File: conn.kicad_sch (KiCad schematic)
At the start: 59 parts, among them J1 JST_1x02, J10 MicroFit_2x04, J11 MLX_1x03, J12 MLX_1x03, J13 JST_1x04, J14 JST_1x04, J15 JST_1x04, J16 JST_1x04, J17 JST_1x02, J5 JST_01x02, J7 JST_B6B-XH, J8 MicroFit_2x04, J9 MicroFit_2x04, SW2 !EMERG STOP!

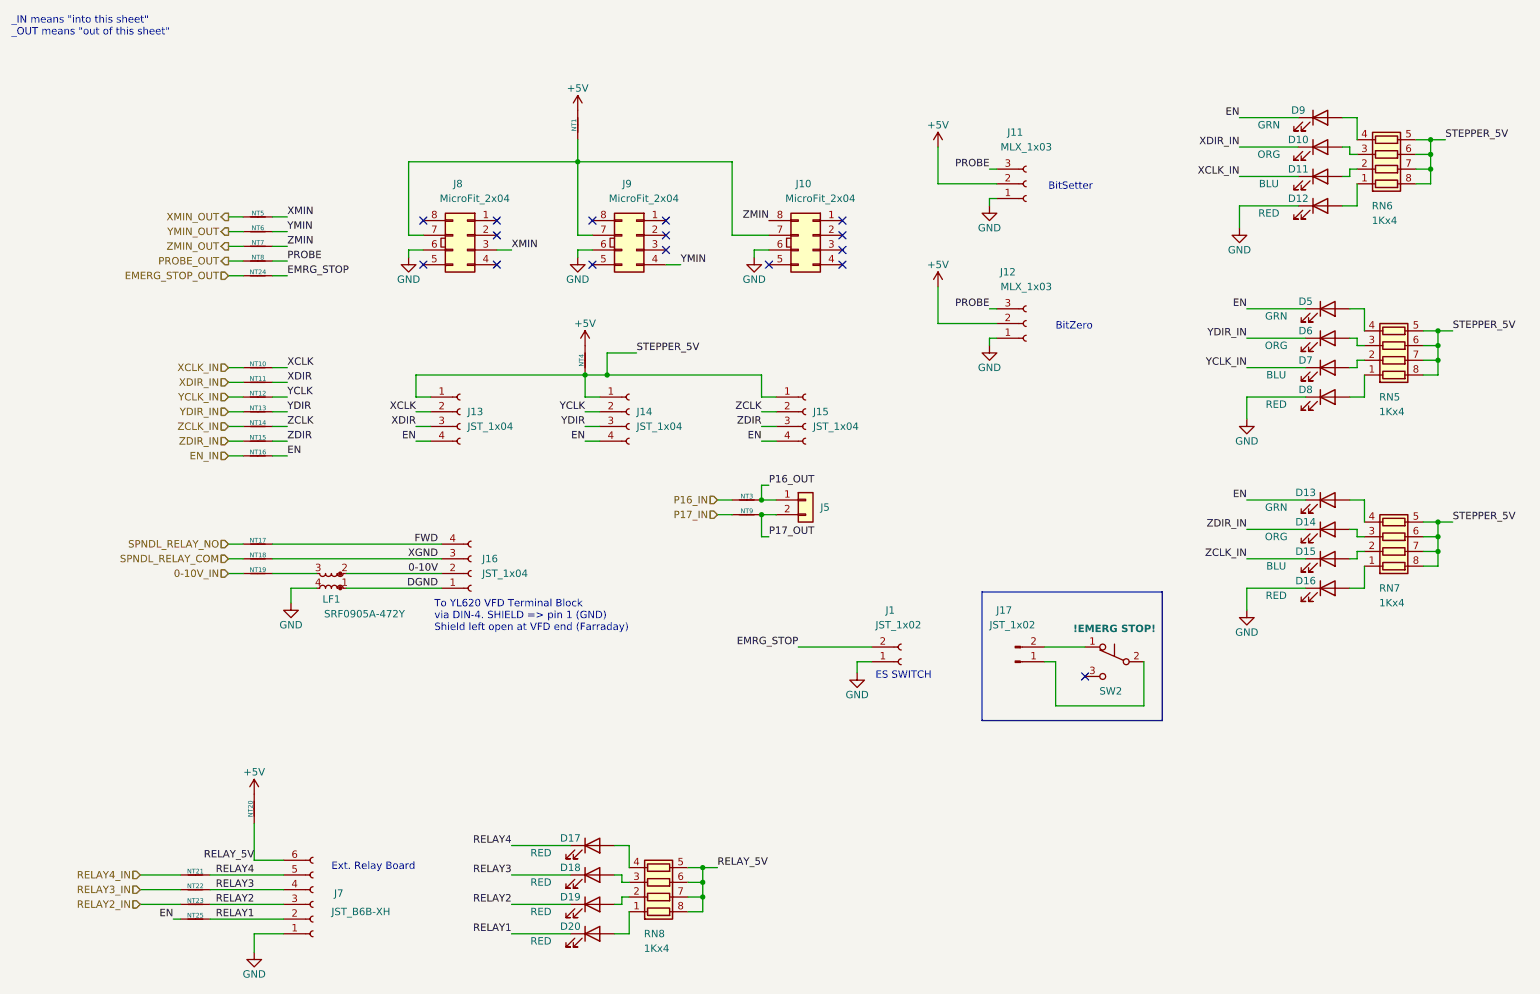
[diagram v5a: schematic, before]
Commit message: Resistor networks changed to 0603 'cause JLCPCB has those as 'basic parts' & aunch of tweaks. (WIP)
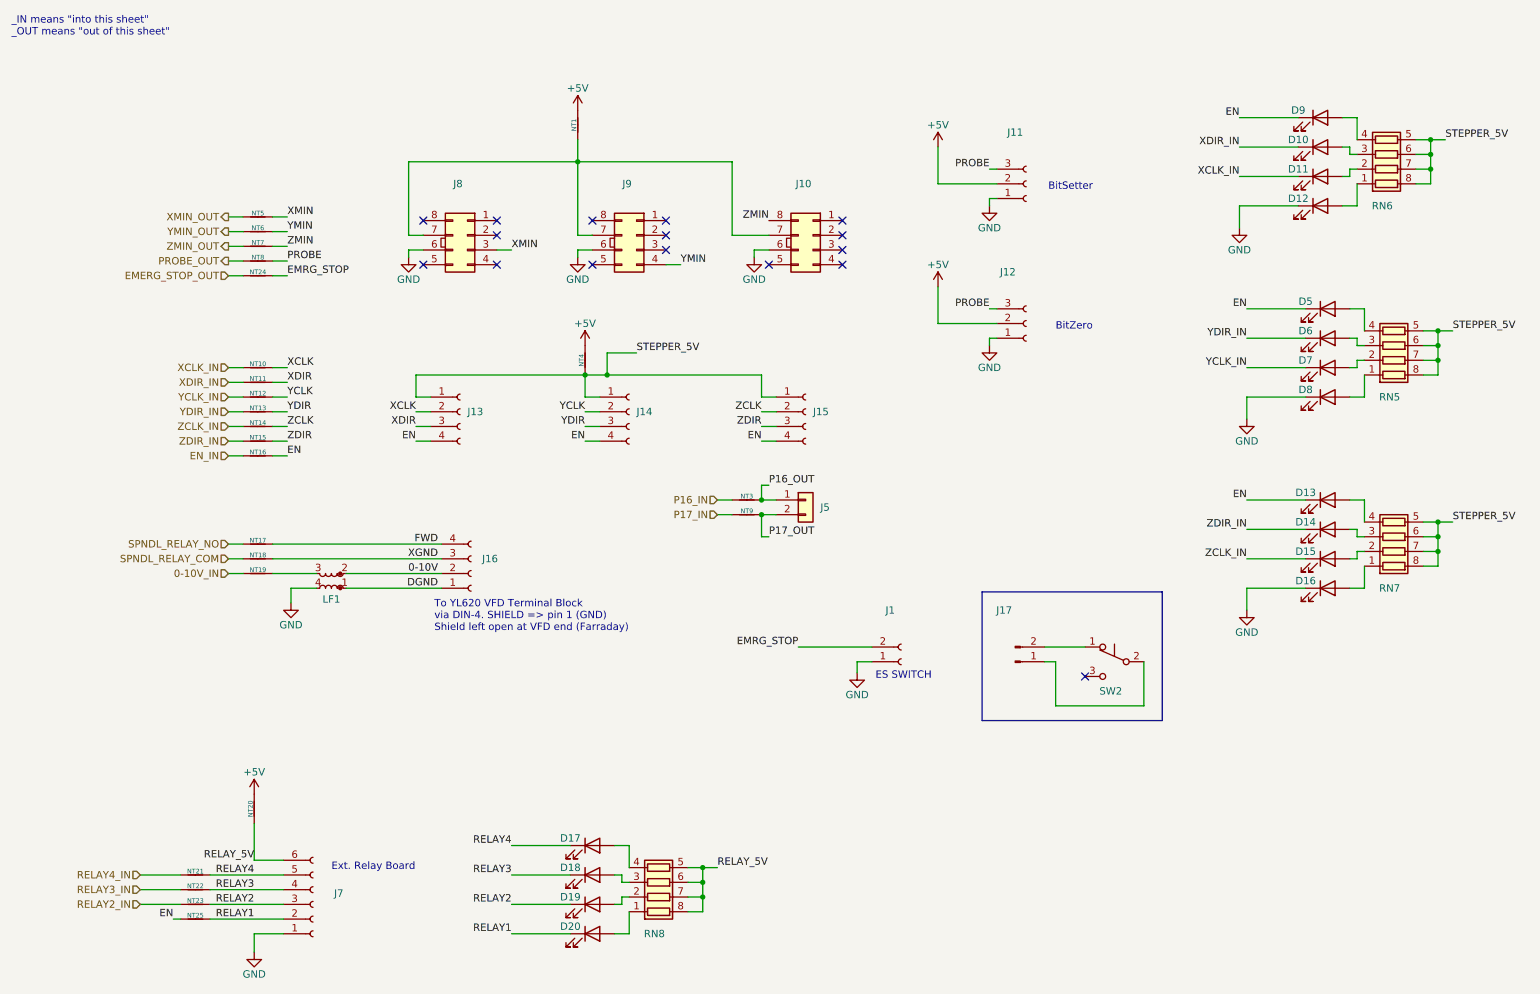
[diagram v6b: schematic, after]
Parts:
- D10, D14, D6: value ORG -> (none); footprint LED_SMD:LED_0402_1005Metric -> (none)
- D11, D15, D7: value BLU -> (none); footprint LED_SMD:LED_0402_1005Metric -> (none)
- D12, D16, D17, D18, D19, D20, D8: value RED -> (none); footprint LED_SMD:LED_0402_1005Metric -> (none)
- D13, D5, D9: value GRN -> (none); footprint LED_SMD:LED_0402_1005Metric -> (none)
- J1: value JST_1x02 -> (none); footprint Connector_JST:JST_EH_S2B-EH_1x02_P2.50mm_Horizontal -> (none)
- J10, J8, J9: value MicroFit_2x04 -> (none); footprint Connector_Molex:Molex_Micro-Fit_3.0_43045-0812_2x04_P3.00mm_Vertical -> (none)
- J11, J12: value MLX_1x03 -> (none); footprint Connector_Molex:Molex_KK-254_AE-6410-03A_1x03_P2.54mm_Vertical -> (none)
- J13, J14, J15, J16: value JST_1x04 -> (none); footprint Connector_JST:JST_EH_S4B-EH_1x04_P2.50mm_Horizontal -> (none)
- J17: value JST_1x02 -> (none); footprint Connector_Molex:Molex_KK-254_AE-6410-03A_1x02_P2.54mm_Vertical -> (none)
- J5: value JST_01x02 -> (none); footprint Connector_JST:JST_EH_B2B-EH-A_1x02_P2.50mm_Vertical -> (none)
- J7: value JST_B6B-XH -> (none); footprint Connector_JST:JST_EH_S6B-EH_1x06_P2.50mm_Horizontal -> (none)
- LF1: value SRF0905A-472Y -> (none); footprint Filter:Filter_Bourns_SRF0905_6.0x9.2mm -> (none)
- NT1, NT20, NT4: value DNI -> (none); footprint _footprints:NetTie-2_SMD_Pad1.0mm -> (none)
- NT10, NT11, NT12, NT13, NT14, NT15, NT16, NT17, NT18, NT19, NT21, NT22, NT23, NT24, NT25, NT3, NT5, NT6, NT7, NT8, NT9: value DNI -> (none); footprint _footprints:NetTie-2_SMD_Pad0.3mm -> (none)
- RN5, RN6, RN7, RN8: value 1Kx4 -> (none); footprint Resistor_SMD:R_Array_Convex_4x0402 -> (none); Element14 1768299 -> (none); JLCPCB (none) -> C20197; M.Part# (none) -> 4D03WGJ0102T5E; MOQ (none) -> 1
- SW2: value !EMERG STOP! -> (none)

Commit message: temp
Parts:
- D10, D14, D6: value (none) -> ORG
- D11, D15, D7: value (none) -> BLU
- D12, D16, D17, D18, D19, D20, D8: value (none) -> RED
- D13, D5, D9: value (none) -> GRN
- J1: value (none) -> JST_1x02; footprint (none) -> Connector_JST:JST_XH_S2B-XH-A-1_1x02_P2.50mm_Horizontal; E14MFR# (none) -> S2B-XH-A-1(LF)(SN); JLCPART (none) -> C163035
- J10, J8, J9: value (none) -> MicroFit_2x04; E14PART (none) -> 1654450; Element14 1654450 -> (none)
- J11, J12: value (none) -> MLX_1x03; E14PART (none) -> 1462950; Element14 1462950 -> (none)
- J13, J14, J15, J16: value (none) -> JST_1x04; E14PART (none) -> 1516278; Element14 1516278 -> (none)
- J17: value (none) -> JST_1x02_P; E14PART (none) -> 1462950; Element14 1462950 -> (none)
- J5: value (none) -> JST_01x02; footprint (none) -> Connector_JST:JST_XH_B2B-XH-AM_1x02_P2.50mm_Vertical; JLCMFR# (none) -> B2B-XH-AM(LF)(SN); JLCPART (none) -> C161869; JLCPCB C474892 -> (none); M.Part# KF350-3.5-2P -> (none); Manufacturer Cixi Kefa Elec -> (none)
- J7: value (none) -> JST_B6B-XH; E14PART (none) -> 1516282; Element14 1516282 -> (none)
- LF1: value (none) -> SRF0905A-472Y; E14PART (none) -> 2455014; Element14 2455014 -> (none)
- NT1, NT10, NT11, NT12, NT13, NT14, NT15, NT16, NT17, NT18, NT19, NT20, NT21, NT22, NT23, NT24, NT25, NT3, NT4, NT5, NT6, NT7, NT8, NT9: value (none) -> DNI
- RN5, RN6, RN7, RN8: value (none) -> 1Kx4; JLCMFR# (none) -> 4D03WGJ0102T5E; JLCPART (none) -> C20197; JLCPCB C20197 -> (none); M.Part# 4D03WGJ0102T5E -> (none)
- SW2: value (none) -> !EMERG STOP!
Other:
- moved on the sheet: J5

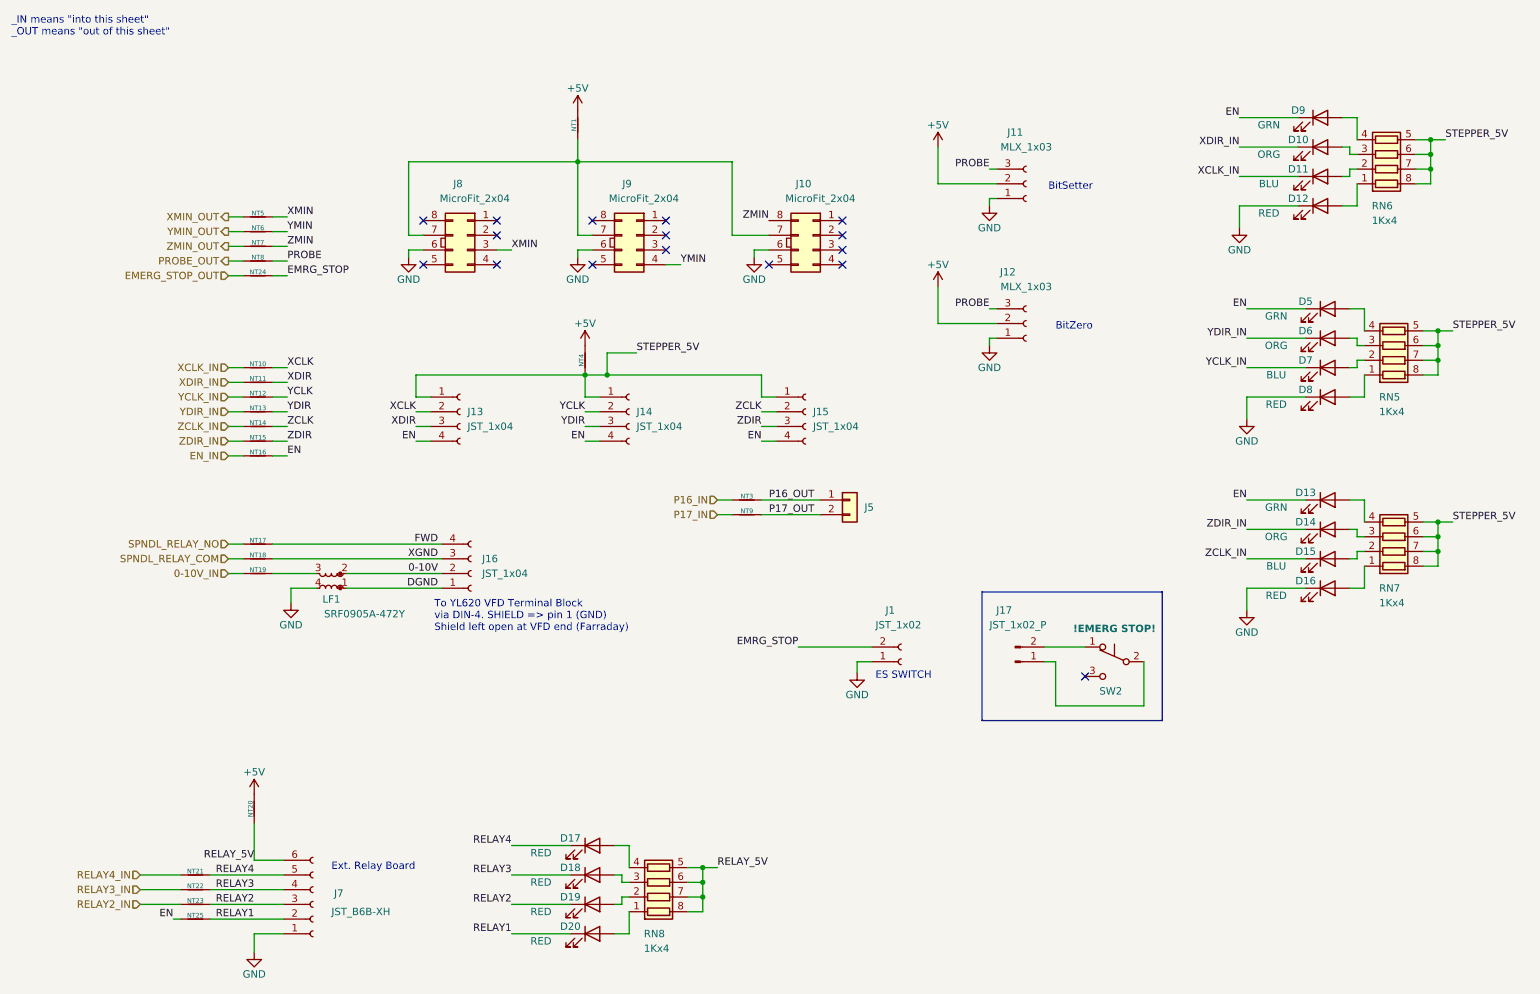
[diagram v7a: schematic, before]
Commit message: Scary file corruption turns out to be just bugs in eschema.
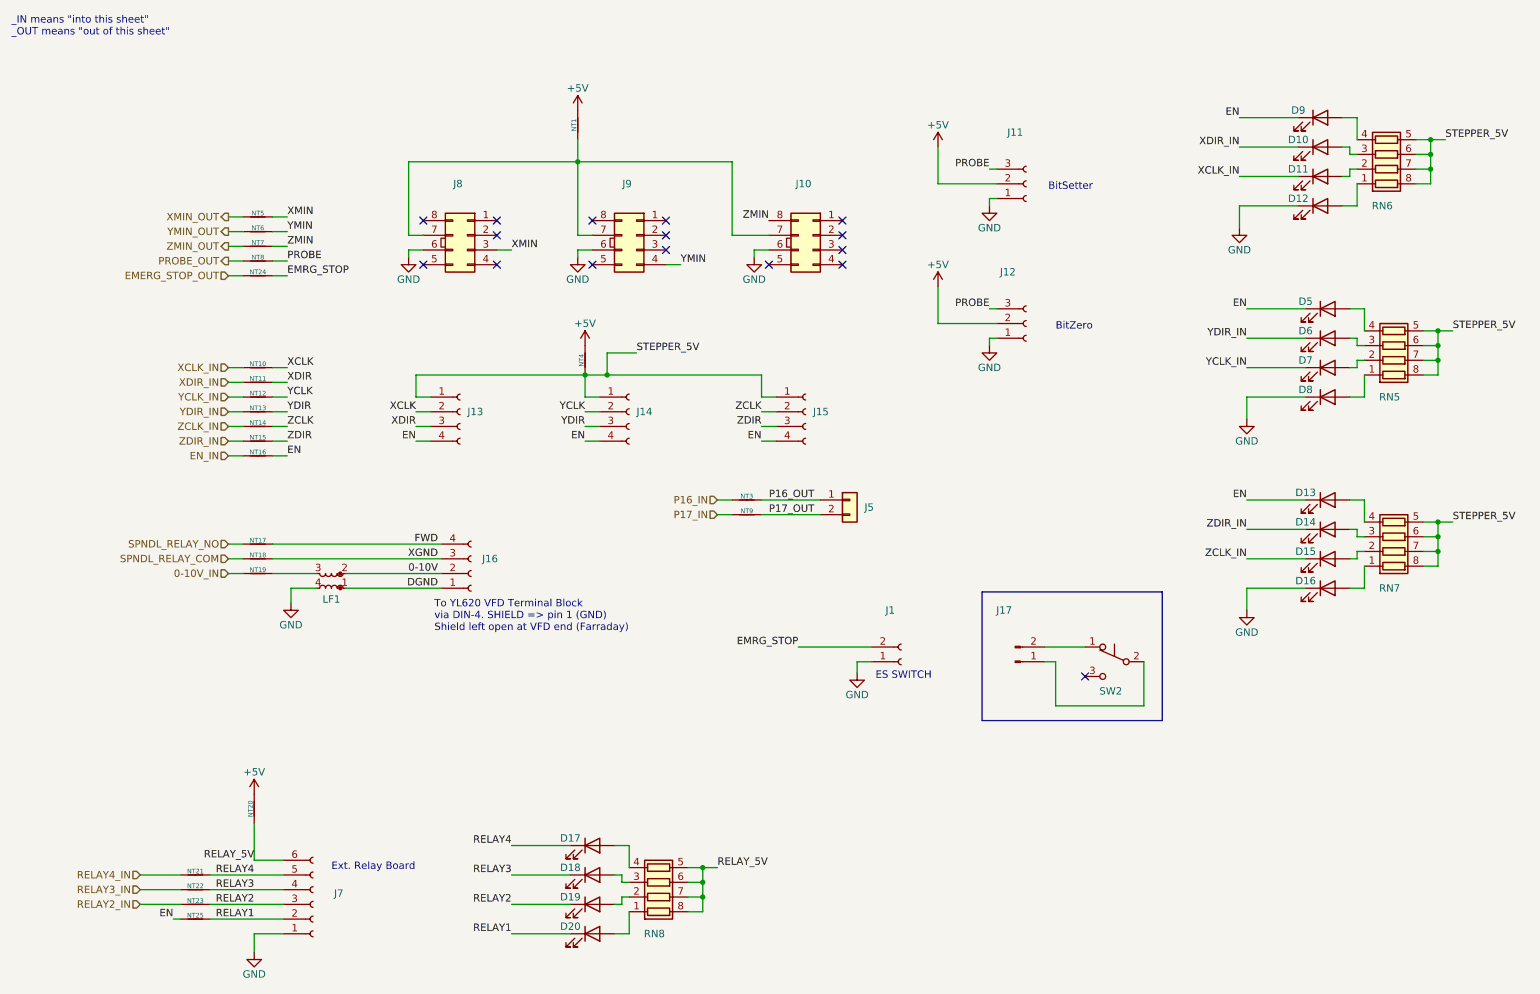
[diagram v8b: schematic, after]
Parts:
- D10, D14, D6: value ORG -> (none)
- D11, D15, D7: value BLU -> (none)
- D12, D16, D17, D18, D19, D20, D8: value RED -> (none)
- D13, D5, D9: value GRN -> (none)
- J1: value JST_1x02 -> (none); footprint Connector_JST:JST_XH_S2B-XH-A-1_1x02_P2.50mm_Horizontal -> (none)
- J10, J8, J9: value MicroFit_2x04 -> (none)
- J11, J12: value MLX_1x03 -> (none)
- J13, J14, J15, J16: value JST_1x04 -> (none)
- J17: value JST_1x02_P -> (none)
- J5: value JST_01x02 -> (none); footprint Connector_JST:JST_XH_B2B-XH-AM_1x02_P2.50mm_Vertical -> (none)
- J7: value JST_B6B-XH -> (none)
- LF1: value SRF0905A-472Y -> (none)
- NT1, NT10, NT11, NT12, NT13, NT14, NT15, NT16, NT17, NT18, NT19, NT20, NT21, NT22, NT23, NT24, NT25, NT3, NT4, NT5, NT6, NT7, NT8, NT9: value DNI -> (none)
- RN5, RN6, RN7, RN8: value 1Kx4 -> (none)
- SW2: value !EMERG STOP! -> (none)
